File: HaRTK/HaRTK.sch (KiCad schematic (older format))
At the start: 8 parts

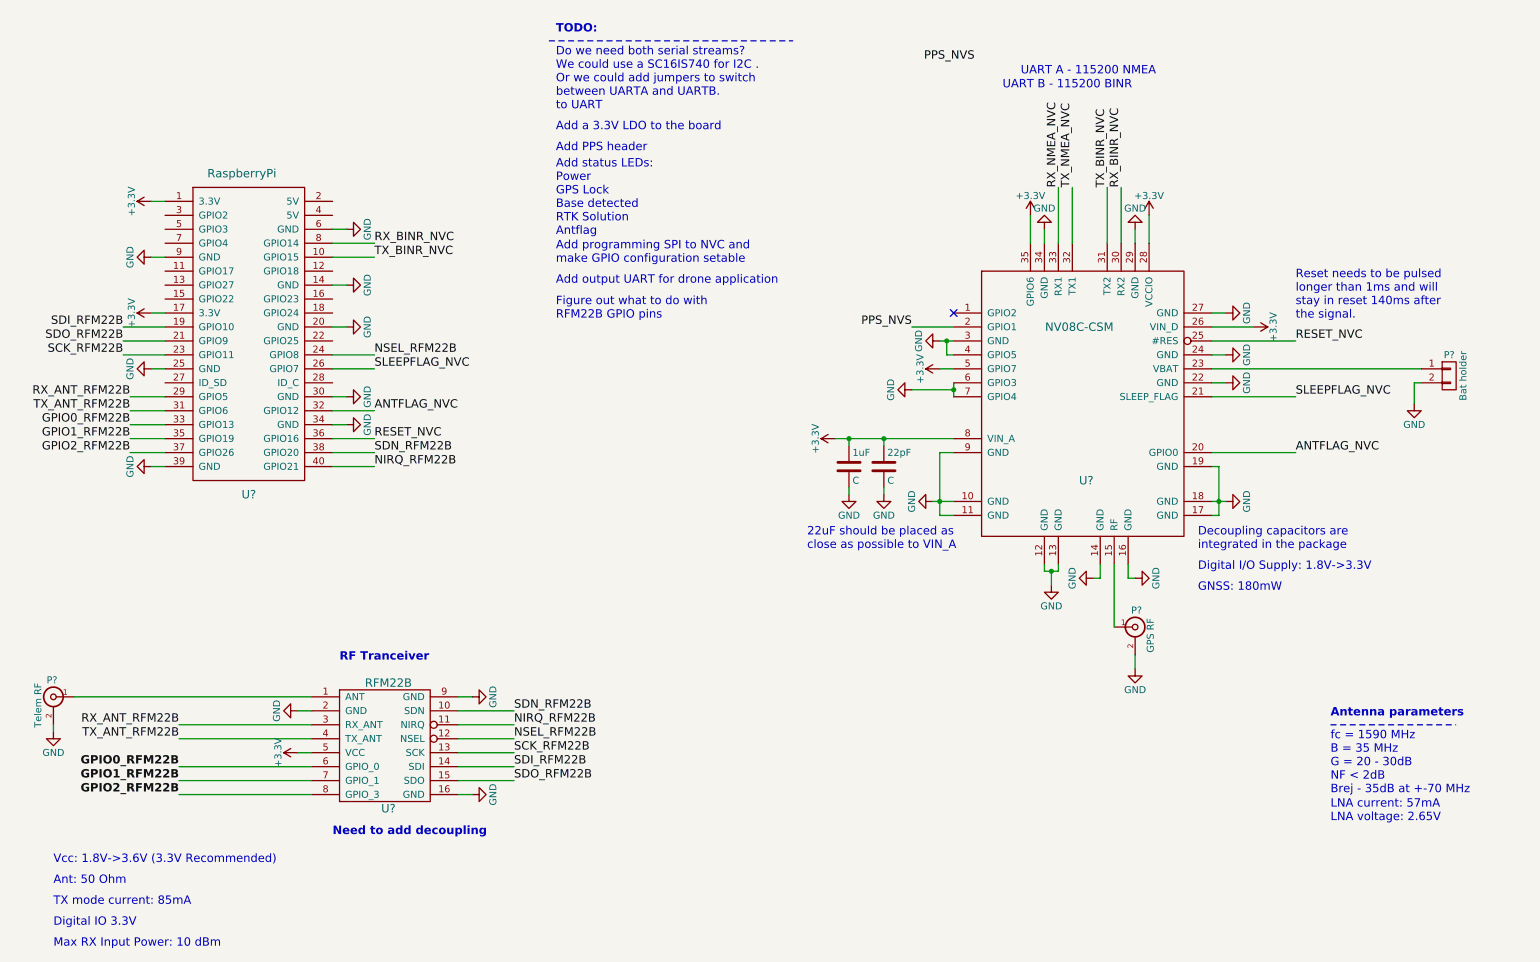
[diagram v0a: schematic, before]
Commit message: Added datasheets and finished schematic
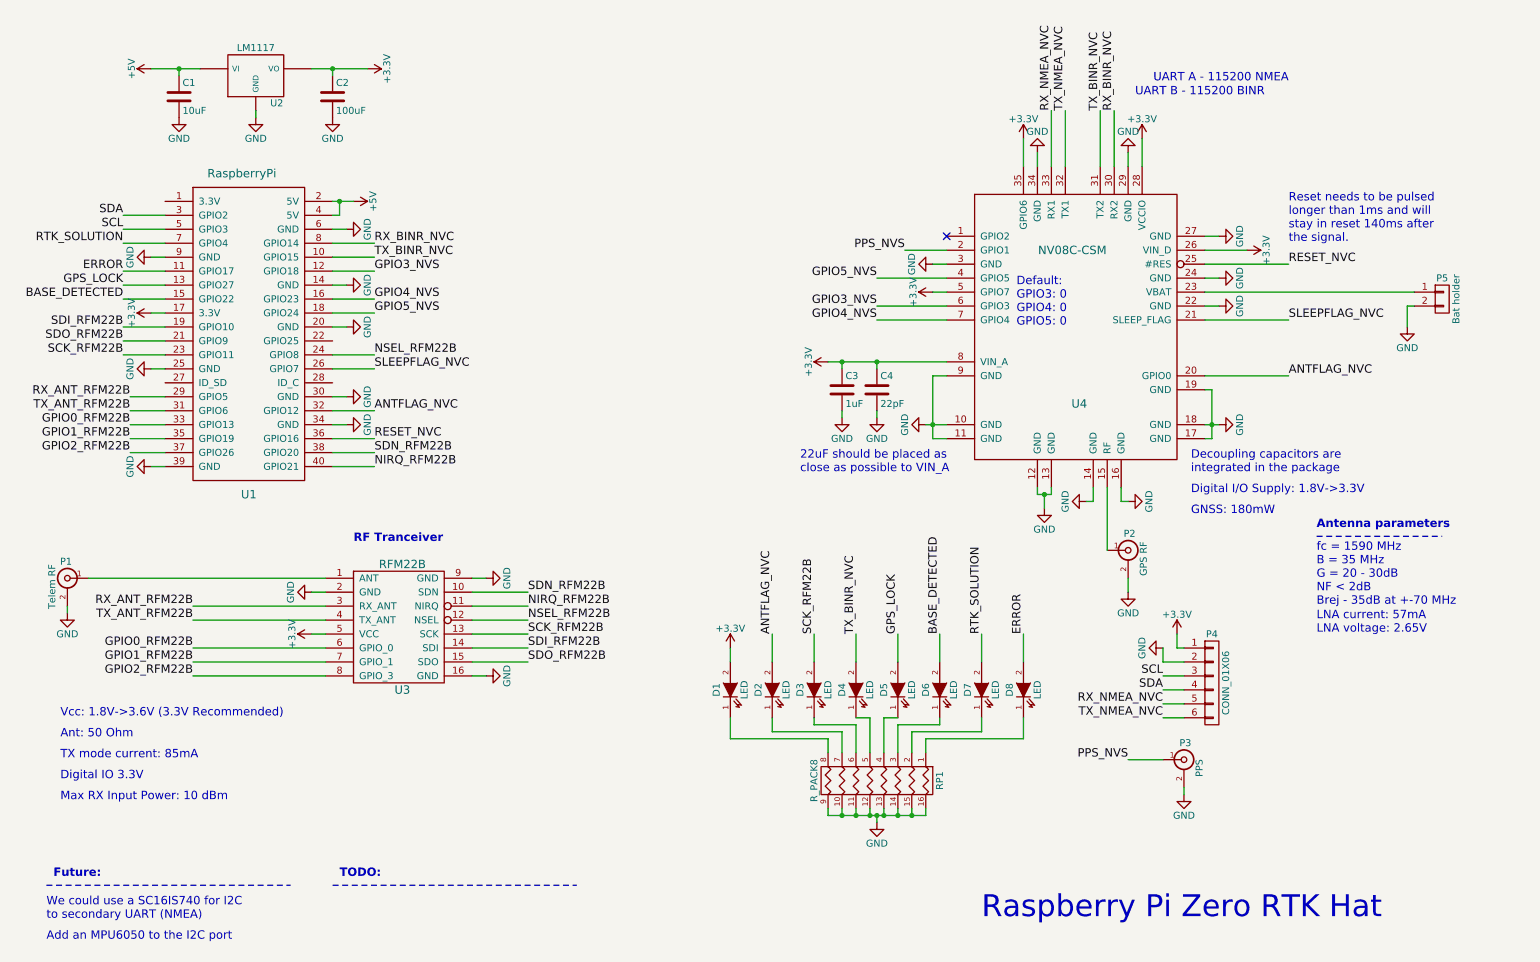
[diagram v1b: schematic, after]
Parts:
- added C1: 10uF, symbol C
- added C2: 100uF, symbol C
- added D1, D2, D3, D4, D5, D6, D7, D8: LED, Resistors_SMD:R_0805_HandSoldering, symbol LED
- added P3: PPS, symbol BNC
- added P4: CONN_01X06, Pin_Headers:Pin_Header_Angled_1x06, symbol CONN_01X06
- added RP1: R_PACK8, symbol R_PACK8
- added U2: LM1117, symbol 7805
- C3: renamed from 1uF; value C -> 1uF; footprint (none) -> Resistors_SMD:R_0805_HandSoldering
- C4: renamed from 22pF; value C -> 22pF; footprint (none) -> Resistors_SMD:R_0805_HandSoldering
- U1: renamed from U?; footprint (none) -> Pin_Headers:Pin_Header_Straight_2x20
- gave numbers to parts that had none: 5
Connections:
- net +3V3: now also C2.1, D1.2 (A), P4.1 (P1), U2.VO; no longer U1.1 (3.3V)
- net ANTFLAG_NVC: now also D2.2 (A)
- net GND: now also C1.2, C2.2, P3.2 (Ext), P4.2 (P2), RP1.10 (R7), RP1.11 (R6), RP1.12 (R5), RP1.13 (R4), RP1.14 (R3), RP1.15 (R2), RP1.16 (R1), RP1.9 (R8), U2.GND; no longer U4.4 (GPIO5), U4.6 (GPIO3), U4.7 (GPIO4)
- net PPS_NVS: now also P3.1 (In)
- net RX_NMEA_NVC: now also P4.5 (P5)
- net SCK_RFM22B: now also D3.2 (A)
- net TX_BINR_NVC: now also D4.2 (A)
- net TX_NMEA_NVC: now also P4.6 (P6)
- net ERROR: now reaches U1.11 (GPIO17)
- net ERROR: now also D8.2 (A)
- net GPIO3_NVS: now reaches U1.12 (GPIO18)
- net GPIO3_NVS: now also U4.6 (GPIO3)
- net GPS_LOCK: now reaches U1.13 (GPIO27)
- net GPS_LOCK: now also D5.2 (A)
- net BASE_DETECTED: now reaches U1.15 (GPIO22)
- net BASE_DETECTED: now also D6.2 (A)
- net GPIO4_NVS: now reaches U1.16 (GPIO23)
- net GPIO4_NVS: now also U4.7 (GPIO4)
- net GPIO5_NVS: now reaches U1.18 (GPIO24)
- net GPIO5_NVS: now also U4.4 (GPIO5)
- net +5V: now reaches U1.2 (5V)
- net +5V: now also U1.4 (5V), C1.1, U2.VI
- net SDA: now reaches U1.3 (GPIO2)
- net SDA: now also P4.4 (P4)
- net SCL: now reaches U1.5 (GPIO3)
- net SCL: now also P4.3 (P3)
- net RTK_SOLUTION: now reaches U1.7 (GPIO4)
- net RTK_SOLUTION: now also D7.2 (A)
- new net: D1.1 (K), RP1.8 (P8)
- new net: D2.1 (K), RP1.7 (P7)
- new net: D3.1 (K), RP1.6 (P6)
- new net: D4.1 (K), RP1.5 (P5)
- new net: D5.1 (K), RP1.4 (P4)
- new net: D6.1 (K), RP1.3 (P3)
- new net: D8.1 (K), RP1.1 (P1)
- new net: D7.1 (K), RP1.2 (P2)
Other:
- note added: "Add an MPU6050 to the I2C port\n"
- note added: "Default: \nGPIO3: 0\nGPIO4: 0\nGPIO5: 0"
- note added: "Future:"
- note added: "Raspberry Pi Zero RTK Hat"
- note added: "We could use a SC16IS740 for I2C\nto secondary UART (NMEA)"
- note removed: "Add PPS header"
- note removed: "Add a 3.3V LDO to the board"
- note removed: "Add output UART for drone application"
- note removed: "Add programming SPI to NVC and \nmake GPIO configuration setable"
- note removed: "Add status LEDs:\nPower\nGPS Lock\nBase detected\nRTK Solution\nAntflag"
- note removed: "Do we need both serial streams?\nWe could use a SC16IS740 for I2C .\nOr we could add jumpers to switch \nbetween UARTA and UARTB.\nto UART"
- note removed: "Figure out what to do with\nRFM22B GPIO pins"
- note removed: "Need to add decoupling\n"
- moved on the sheet: C3, C4, P1, P2, P5, U3, U4

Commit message: Started PCB Layout
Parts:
- C1, C2: footprint (none) -> Capacitors_SMD:C_1206_HandSoldering
- C3, C4: footprint Resistors_SMD:R_0805_HandSoldering -> Capacitors_SMD:C_0805_HandSoldering
- D1, D2, D3, D4, D5, D6, D7, D8: footprint Resistors_SMD:R_0805_HandSoldering -> LEDs:LED_0805
- P1, P2, P3: footprint (none) -> Misc:RightAngleSMA
- P5: footprint (none) -> Misc:Batholder1220
- RP1: footprint (none) -> Resistors_SMD:R_Array_Convex_8x0602
- U2: footprint (none) -> TO_SOT_Packages_SMD:SOT-223
- U3: footprint (none) -> RFM22B:RFM22B
- U4: footprint (none) -> NV08C-CSM:NV08C-CSM
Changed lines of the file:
@@
 F 0 "U4" H 8100 2050 60  0000 C CNN
 F 1 "NV08C-CSM" H 8050 3150 60  0000 C CNN
-F 2 "" H 7100 4000 60  0001 C CNN
+F 2 "NV08C-CSM:NV08C-CSM" H 7100 4000 60  0001 C CNN
 F 3 "" H 7100 4000 60  0000 C CNN
 	1    8100 2650
@@
 F 0 "U3" H 3250 4200 60  0000 C CNN
 F 1 "RFM22B" H 3250 5100 60  0000 C CNN
-F 2 "" H 3300 4750 60  0001 C CNN
+F 2 "RFM22B:RFM22B" H 3300 4750 60  0001 C CNN
 F 3 "" H 3300 4750 60  0000 C CNN
 	1    3250 4750
@@
 F 0 "P1" H 860 4620 50  0000 C CNN
 F 1 "Telem RF" V 960 4440 50  0000 C CNN
-F 2 "" H 850 4500 50  0001 C CNN
+F 2 "Misc:RightAngleSMA" H 850 4500 50  0001 C CNN
 F 3 "" H 850 4500 50  0000 C CNN
 	1    850  4500
@@
 F 0 "C4" H 6675 3250 50  0000 L CNN
 F 1 "22pF" H 6675 3050 50  0000 L CNN
-F 2 "Resistors_SMD:R_0805_HandSoldering" H 6688 3000 50  0001 C CNN
+F 2 "Capacitors_SMD:C_0805_HandSoldering" H 6688 3000 50  0001 C CNN
 F 3 "" H 6650 3150 50  0000 C CNN
 	1    6650 3150
@@
 F 0 "C3" H 6425 3250 50  0000 L CNN
 F 1 "1uF" H 6425 3050 50  0000 L CNN
-F 2 "Resistors_SMD:R_0805_HandSoldering" H 6438 3000 50  0001 C CNN
+F 2 "Capacitors_SMD:C_0805_HandSoldering" H 6438 3000 50  0001 C CNN
 F 3 "" H 6400 3150 50  0000 C CNN
 	1    6400 3150
@@
 F 0 "P5" H 10700 2650 50  0000 C CNN
 F 1 "Bat holder" V 10800 2500 50  0000 C CNN
-F 2 "" H 10700 2500 50  0001 C CNN
+F 2 "Misc:Batholder1220" H 10700 2500 50  0001 C CNN
 F 3 "" H 10700 2500 50  0000 C CNN
 	1    10700 2500
@@
 F 0 "P2" H 8460 4420 50  0000 C CNN
 F 1 "GPS RF" V 8560 4240 50  0000 C CNN
-F 2 "" H 8450 4300 50  0001 C CNN
+F 2 "Misc:RightAngleSMA" H 8450 4300 50  0001 C CNN
 F 3 "" H 8450 4300 50  0000 C CNN
 	1    8450 4300
@@
 F 0 "D1" H 5600 5400 50  0000 C CNN
 F 1 "LED" H 5600 5200 50  0000 C CNN
-F 2 "Resistors_SMD:R_0805_HandSoldering" H 5600 5300 50  0001 C CNN
+F 2 "LEDs:LED_0805" H 5600 5300 50  0001 C CNN
 F 3 "" H 5600 5300 50  0000 C CNN
 	1    5600 5300
@@
 F 0 "D2" H 5900 5400 50  0000 C CNN
 F 1 "LED" H 5900 5200 50  0000 C CNN
-F 2 "Resistors_SMD:R_0805_HandSoldering" H 5900 5300 50  0001 C CNN
+F 2 "LEDs:LED_0805" H 5900 5300 50  0001 C CNN
 F 3 "" H 5900 5300 50  0000 C CNN
 	1    5900 5300
@@
 F 0 "D3" H 6200 5400 50  0000 C CNN
 F 1 "LED" H 6200 5200 50  0000 C CNN
-F 2 "Resistors_SMD:R_0805_HandSoldering" H 6200 5300 50  0001 C CNN
+F 2 "LEDs:LED_0805" H 6200 5300 50  0001 C CNN
 F 3 "" H 6200 5300 50  0000 C CNN
 	1    6200 5300
@@
 F 0 "D4" H 6500 5400 50  0000 C CNN
 F 1 "LED" H 6500 5200 50  0000 C CNN
-F 2 "Resistors_SMD:R_0805_HandSoldering" H 6500 5300 50  0001 C CNN
+F 2 "LEDs:LED_0805" H 6500 5300 50  0001 C CNN
 F 3 "" H 6500 5300 50  0000 C CNN
 	1    6500 5300
@@
 F 0 "D5" H 6800 5400 50  0000 C CNN
 F 1 "LED" H 6800 5200 50  0000 C CNN
-F 2 "Resistors_SMD:R_0805_HandSoldering" H 6800 5300 50  0001 C CNN
+F 2 "LEDs:LED_0805" H 6800 5300 50  0001 C CNN
 F 3 "" H 6800 5300 50  0000 C CNN
 	1    6800 5300
@@
 F 0 "D6" H 7100 5400 50  0000 C CNN
 F 1 "LED" H 7100 5200 50  0000 C CNN
-F 2 "Resistors_SMD:R_0805_HandSoldering" H 7100 5300 50  0001 C CNN
+F 2 "LEDs:LED_0805" H 7100 5300 50  0001 C CNN
 F 3 "" H 7100 5300 50  0000 C CNN
 	1    7100 5300
@@
 F 0 "RP1" H 6650 6400 50  0000 C CNN
 F 1 "R_PACK8" H 6650 5500 50  0000 C CNN
-F 2 "" H 6650 5950 50  0001 C CNN
+F 2 "Resistors_SMD:R_Array_Convex_8x0602" H 6650 5950 50  0001 C CNN
 F 3 "" H 6650 5950 50  0000 C CNN
 	1    6650 5950
@@
 F 0 "D7" H 7400 5400 50  0000 C CNN
 F 1 "LED" H 7400 5200 50  0000 C CNN
-F 2 "Resistors_SMD:R_0805_HandSoldering" H 7400 5300 50  0001 C CNN
+F 2 "LEDs:LED_0805" H 7400 5300 50  0001 C CNN
 F 3 "" H 7400 5300 50  0000 C CNN
 	1    7400 5300
@@
 F 0 "D8" H 7700 5400 50  0000 C CNN
 F 1 "LED" H 7700 5200 50  0000 C CNN
-F 2 "Resistors_SMD:R_0805_HandSoldering" H 7700 5300 50  0001 C CNN
+F 2 "LEDs:LED_0805" H 7700 5300 50  0001 C CNN
 F 3 "" H 7700 5300 50  0000 C CNN
 	1    7700 5300
@@
 F 0 "U2" H 2350 704 50  0000 C CNN
 F 1 "LM1117" H 2200 1100 50  0000 C CNN
-F 2 "" H 2200 900 50  0001 C CNN
+F 2 "TO_SOT_Packages_SMD:SOT-223" H 2200 900 50  0001 C CNN
 F 3 "" H 2200 900 50  0000 C CNN
 	1    2200 900
@@
 F 0 "C1" H 1675 1150 50  0000 L CNN
 F 1 "10uF" H 1675 950 50  0000 L CNN
-F 2 "" H 1688 900 50  0001 C CNN
+F 2 "Capacitors_SMD:C_1206_HandSoldering" H 1688 900 50  0001 C CNN
 F 3 "" H 1650 1050 50  0000 C CNN
 	1    1650 1050
@@
 F 0 "C2" H 2775 1150 50  0000 L CNN
 F 1 "100uF" H 2775 950 50  0000 L CNN
-F 2 "" H 2788 900 50  0001 C CNN
+F 2 "Capacitors_SMD:C_1206_HandSoldering" H 2788 900 50  0001 C CNN
 F 3 "" H 2750 1050 50  0000 C CNN
 	1    2750 1050
@@
 F 0 "P3" H 8860 5920 50  0000 C CNN
 F 1 "PPS" V 8960 5740 50  0000 C CNN
-F 2 "" H 8850 5800 50  0001 C CNN
+F 2 "Misc:RightAngleSMA" H 8850 5800 50  0001 C CNN
 F 3 "" H 8850 5800 50  0000 C CNN
 	1    8850 5800

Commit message: First revision
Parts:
- removed C3: 1uF, Capacitors_SMD:C_0805_HandSoldering, symbol C
- removed C4: 22pF, Capacitors_SMD:C_0805_HandSoldering, symbol C
- U2: symbol 7805 -> 7805-RESCUE-HaRTK
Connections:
- net +3V3: now also U2.3 (VO); no longer U2.VO
- net +5V: now also U2.1 (VI); no longer U2.VI
- net GND: now also U2.2 (GND); no longer U2.GND
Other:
- note removed: "22uF should be placed as \nclose as possible to VIN_A\n"
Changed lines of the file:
@@
 EESchema Schematic File Version 2
+LIBS:HaRTK-rescue
 LIBS:power
 LIBS:device
@@
 Text Notes 8900 3750 0    60   ~ 0
 Decoupling capacitors are \nintegrated in the package
-$Comp
-L C C4
-U 1 1 56F306DE
-P 6650 3150
-F 0 "C4" H 6675 3250 50  0000 L CNN
-F 1 "22pF" H 6675 3050 50  0000 L CNN
-F 2 "Capacitors_SMD:C_0805_HandSoldering" H 6688 3000 50  0001 C CNN
-F 3 "" H 6650 3150 50  0000 C CNN
-	1    6650 3150
-	1    0    0    -1
-$EndComp
-$Comp
-L C C3
-U 1 1 56F30763
-P 6400 3150
-F 0 "C3" H 6425 3250 50  0000 L CNN
-F 1 "1uF" H 6425 3050 50  0000 L CNN
-F 2 "Capacitors_SMD:C_0805_HandSoldering" H 6438 3000 50  0001 C CNN
-F 3 "" H 6400 3150 50  0000 C CNN
-	1    6400 3150
-	1    0    0    -1
-$EndComp
-$Comp
-L GND #PWR028
-U 1 1 56F309B6
-P 6650 3350
-F 0 "#PWR028" H 6650 3100 50  0001 C CNN
-F 1 "GND" H 6650 3200 50  0000 C CNN
-F 2 "" H 6650 3350 50  0000 C CNN
-F 3 "" H 6650 3350 50  0000 C CNN
-	1    6650 3350
-	1    0    0    -1
-$EndComp
-$Comp
-L GND #PWR029
-U 1 1 56F30A20
-P 6400 3350
-F 0 "#PWR029" H 6400 3100 50  0001 C CNN
-F 1 "GND" H 6400 3200 50  0000 C CNN
-F 2 "" H 6400 3350 50  0000 C CNN
-F 3 "" H 6400 3350 50  0000 C CNN
-	1    6400 3350
-	1    0    0    -1
-$EndComp
-Text Notes 6100 3750 0    60   ~ 0
-22uF should be placed as \nclose as possible to VIN_A\n
 Text Label 9600 2250 0    60   ~ 0
 RESET_NVC
@@
 	9000 2250 9600 2250
 Wire Wire Line
-	6400 3300 6400 3350
-Wire Wire Line
-	6650 3300 6650 3350
-Connection ~ 6650 2950
-Wire Wire Line
-	6650 3000 6650 2950
-Connection ~ 6400 2950
-Wire Wire Line
-	6400 3000 6400 2950
-Wire Wire Line
 	9300 2150 9000 2150
 Wire Wire Line
@@
 Connection ~ 2800 1800
 $Comp
-L 7805 U2
+L 7805-RESCUE-HaRTK U2
 U 1 1 56FEBB1A
 P 2200 900
